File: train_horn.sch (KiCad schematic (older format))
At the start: 72 parts, among them J1 USB_OTG, J2 PROG, Q1 2N7002, SW1 PLAY, U1 MIC7221, U2 MCP73831, U3 TPS78233DDCR, U4 MSP430FR2000_TSSOP, U5 TPA6211A1

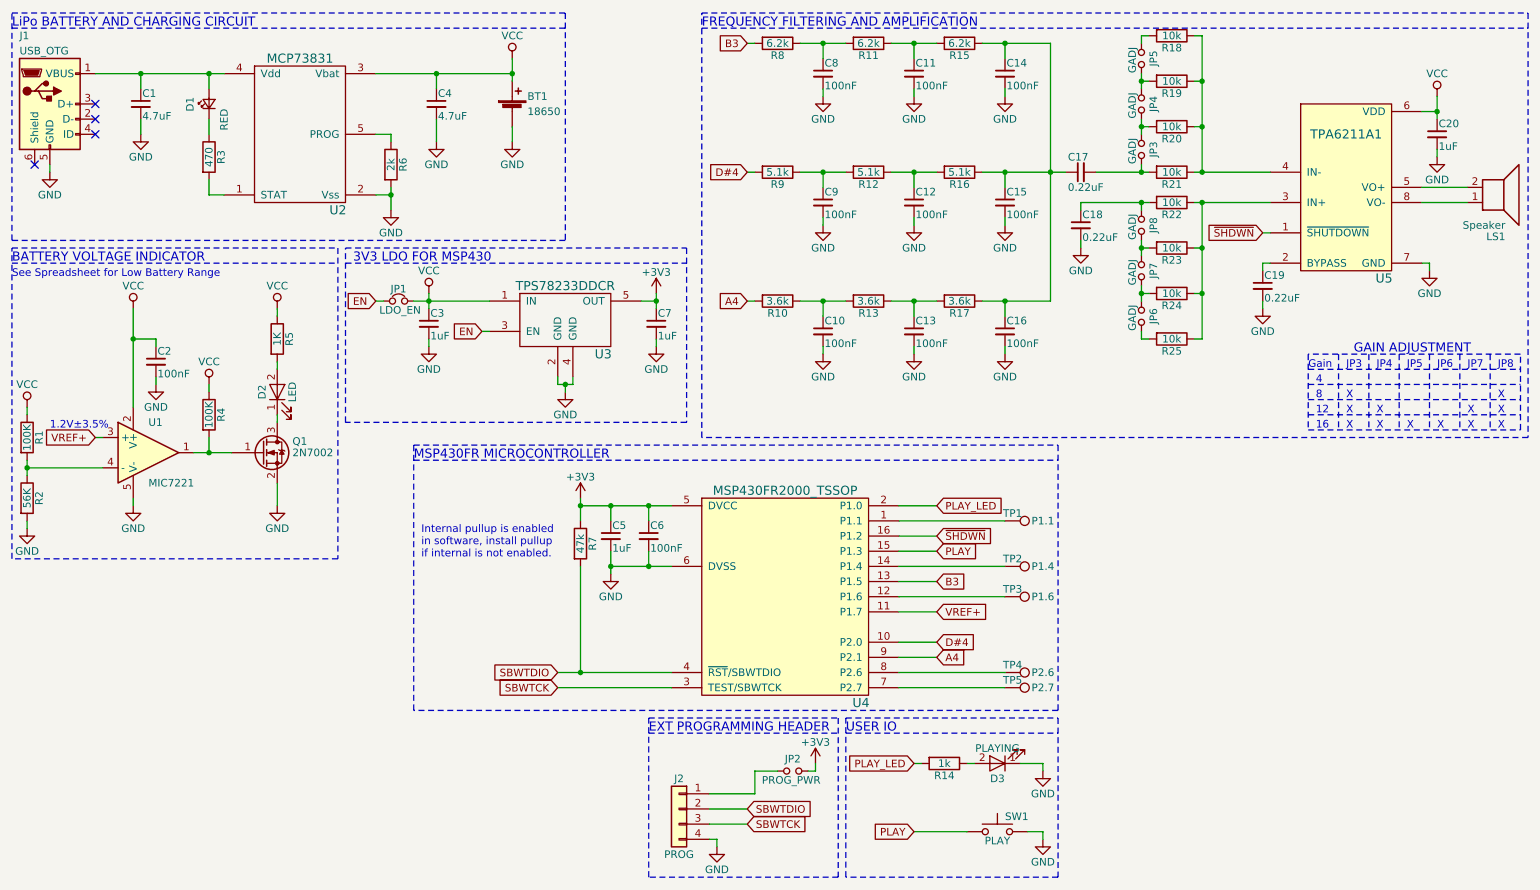
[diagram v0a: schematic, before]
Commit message: update schematic component description fields
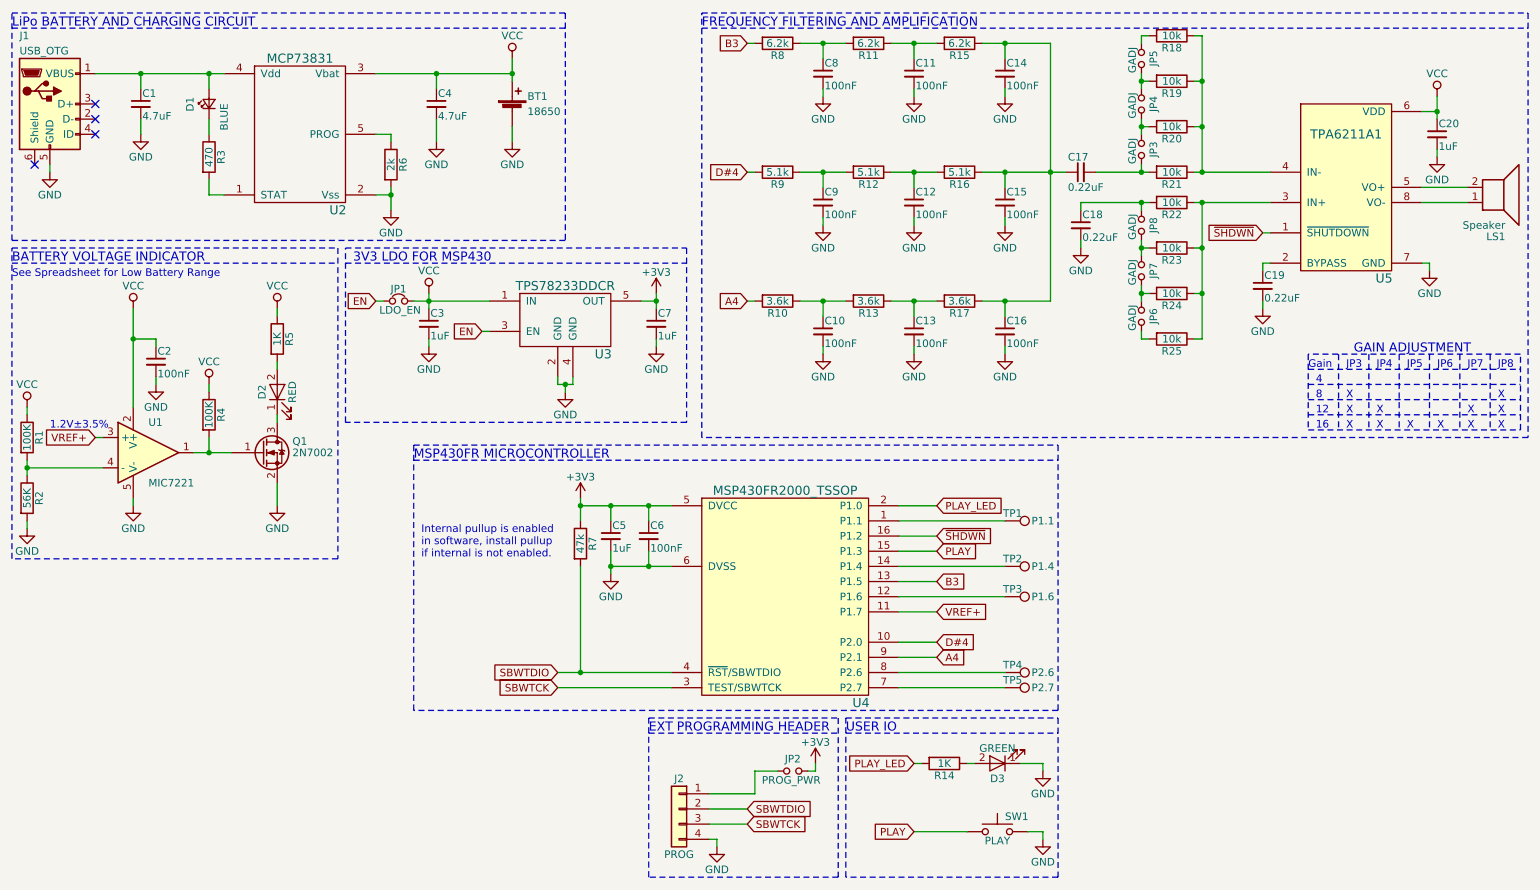
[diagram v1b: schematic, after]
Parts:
- BT1: Description NONE -> HOLDER BATT 18650 1CELL PC PIN; Manufacture NONE -> MPD; Mfg Part Number NONE -> BH-18650-PC-ND; Package NONE -> PC PIN
- C1, C4: Description NONE -> 4.7µF ±10% 6.3V Ceramic Capacitor X5R 0805; Manufacture NONE -> Samsung Electro-Mechanics; Mfg Part Number NONE -> CL21A475KQFNNNG; Package NONE -> 0805
- C10, C2, C6, C8, C9: Description NONE -> CAP CER 0.1UF 16V X7R 0805; Manufacture NONE -> Samsung Electro-Mechanics; Mfg Part Number NONE -> CL21B104KOANNNC; Package NONE -> 0805
- C11, C12, C13, C14, C15, C16: Description (none) -> CAP CER 0.1UF 16V X7R 0805; Manufacture (none) -> Samsung Electro-Mechanics; Mfg Part Number (none) -> CL21B104KOANNNC; Package (none) -> 0805
- C17, C18: Description (none) -> CAP CER 0.22UF 25V X7R 0805; Manufacture (none) -> Samsung Electro-Mechanics; Mfg Part Number (none) -> CL21B224KAFNNNG; Package (none) -> 0805
- C19: Description NONE -> CAP CER 0.22UF 25V X7R 0805; Manufacture NONE -> Samsung Electro-Mechanics; Mfg Part Number NONE -> CL21B224KAFNNNG; Package NONE -> 0805
- C20, C3, C5, C7: Description NONE -> CAP CER 1UF 16V X7R 0805; Manufacture NONE -> Samsung Electro-Mechanics; Mfg Part Number NONE -> CL21B105KOFNNNG; Package NONE -> 0805
- D1: value RED -> BLUE; Description NONE -> Blue 470nm LED Indication; Manufacture NONE -> Wurth Electronics Inc.; Mfg Part Number NONE -> 150080BS75000; Package NONE -> 0805
- D2: value LED -> RED; Description (none) -> LED RED CLEAR 0805 SMD; Manufacture (none) -> Wurth Electronics Inc.; Mfg Part Number (none) -> 150080RS75000; Package (none) -> 0805
- D3: value PLAYING -> GREEN; Description NONE -> LED GREEN CLEAR 0805 SMD; Manufacture NONE -> Wurth Electronics Inc.; Mfg Part Number NONE -> 150080GS75000; Package NONE -> 0805
- J1: Description (none) -> USB - micro B USB 2.0 Receptacle Connector 5 Position Surfa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; Manufacture (none) -> Amphenol; Mfg Part Number (none) -> 10118192-0001LF; Package (none) -> USB MICRO B
- J2: Description NONE -> CONN HEADER 4 POS 2.54; Manufacture NONE -> (none); Mfg Part Number NONE -> (none); Package NONE -> PC PIN
- JP1: Description NONE -> RES SMD 0 OHM JUMPER 1/4W 1206; Manufacture NONE -> Yageo; Mfg Part Number NONE -> RC1206JR-070RL; Package NONE -> 1206
- JP2: Description NONE -> CONN HEADER 2 POS 2.54; Manufacture NONE -> (none); Mfg Part Number NONE -> (none); Package NONE -> PC PIN
- LS1: Description (none) -> 2POS 5MM SCREW TERMINAL BLOCK; Package (none) -> PC PIN
- Q1: Description (none) -> MOSFET N-CH 60V 300MA SOT-23; Manufacture (none) -> Vishay Siliconix; Mfg Part Number (none) -> 2N7002K-T1-E3; Package (none) -> SOT-23
- R1, R4: Description NONE -> RES SMD 100K OHM 1% 1/8W 0805; Manufacture NONE -> Yageo; Mfg Part Number NONE -> RC0805FR-07100KL; Package NONE -> 0805
- R10, R13, R17: Description NONE -> RES SMD 3.6K OHM 0.1% 1/8W 0805; Manufacture NONE -> Panasonic Electronic Components; Mfg Part Number NONE -> ERA-6AEB362V; Package NONE -> 0805
- R11, R15, R8: Description NONE -> RES SMD 6.2K OHM 1% 1/8W 0805; Manufacture NONE -> Yageo; Mfg Part Number NONE -> RC0805FR-076K2L; Package NONE -> 0805
- R12, R16, R9: Description NONE -> RES SMD 5.1K OHM 1% 1/8W 0805; Manufacture NONE -> Yageo; Mfg Part Number NONE -> RC0805FR-075K1L; Package NONE -> 0805
- R14: value 1k -> 1K; Description NONE -> RES SMD 1K OHM 1% 1/8W 0805; Manufacture NONE -> https://www.digikey.com/en/supplier-centers/y/yageo; Mfg Part Number NONE -> RC0805FR-071KL; Package NONE -> 0805
- R18, R19, R20, R21, R22, R23, R24, R25: Description NONE -> RES SMD 10K OHM 1% 1/8W 0805; Manufacture NONE -> Yageo; Mfg Part Number NONE -> RC0805FR-0710KL; Package NONE -> 0805
- R2: Description NONE -> RES SMD 56K OHM 1% 1/8W 0805; Manufacture NONE -> Rohm Semiconductor; Mfg Part Number NONE -> MCR10ERTF5602; Package NONE -> 0805
- R3: Description NONE -> RES SMD 470 OHM 1% 1/8W 0805; Manufacture NONE -> Yageo; Mfg Part Number NONE -> RC0805FR-07470RL; Package NONE -> 0805
- R5: Description NONE -> RES SMD 1K OHM 1% 1/8W 0805; Manufacture NONE -> https://www.digikey.com/en/supplier-centers/y/yageo; Mfg Part Number NONE -> RC0805FR-071KL; Package NONE -> 0805
- R6: Description NONE -> RES SMD 2K OHM 1% 1/8W 0805; Manufacture NONE -> Yageo; Mfg Part Number NONE -> RC0805FR-072KL; Package NONE -> 0805
- R7, TP1, TP2, TP3, TP4, TP5: Description NONE -> (none); Manufacture NONE -> (none); Mfg Part Number NONE -> (none); Package NONE -> (none)
- SW1: Description NONE -> SWITCH TACTILE SPST-NO 0.05A 12V; Manufacture NONE -> Panasonic Electronic Components; Mfg Part Number NONE -> EVQ-P7C01P; Package NONE -> Gull Wing
- U1: Description NONE -> IC COMPARATOR R-R SOT-23-5; Manufacture NONE -> Microchip Technology; Mfg Part Number NONE -> MIC7221YM5-TR; Package NONE -> SOT-23-5
- U3: Description (none) -> IC REG LINEAR 3.3V 150MA SOT23-5; Manufacture (none) -> Texas Instruments; Mfg Part Number (none) -> TPS78233DDCR; Package (none) -> SOT23-5
- U4: Description (none) -> 16 MHZ ULTRA-LOW-POWER MICROCONT; Manufacture (none) -> Texas Instruments; Mfg Part Number (none) -> MSP430FR2000IPW16; Package (none) -> 16-TSSOP
- U5: Description (none) -> IC AMP AUDIO PWR 3.1W MONO 8MSOP; Manufacture (none) -> Texas Instruments; Mfg Part Number (none) -> TPA6211A1DGNR; Package (none) -> 8MSOP

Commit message: clean up component discriptions
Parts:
- C1, C4: Description 4.7µF ±10% 6.3V Ceramic Capacitor X5R 0805 -> CAP CER 4.7UF 6.3V X5R 0805
- J1: Description USB - micro B USB 2.0 Receptacle Connector 5 Position Surfa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 -> CONN USB MICRO B RECPT SMT R/A
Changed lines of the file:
@@
 F 5 "CL21A475KQFNNNG" H 1350 1100 60  0001 C CNN "Mfg Part Number"
 F 6 "0805" H 1350 1100 60  0001 C CNN "Package"
-F 7 "4.7µF ±10% 6.3V Ceramic Capacitor X5R 0805 " H 1350 1100 60  0001 C CNN "Description"
+F 7 "CAP CER 4.7UF 6.3V X5R 0805" H 1350 1100 60  0001 C CNN "Description"
 	1    1350 1100
 	1    0    0    -1
@@
 F 5 "10118192-0001LF" H 750 1100 60  0001 C CNN "Mfg Part Number"
 F 6 "USB MICRO B" H 750 1100 60  0001 C CNN "Package"
-F 7 "USB - micro B USB 2.0 Receptacle Connector 5 Position Surface Mount, Right Angle" H 750 1100 60  0001 C CNN "Description"
+F 7 "CONN USB MICRO B RECPT SMT R/A" H 750 1100 60  0001 C CNN "Description"
 	1    750  1100
 	1    0    0    -1
@@
 F 5 "CL21A475KQFNNNG" H 3300 1100 60  0001 C CNN "Mfg Part Number"
 F 6 "0805" H 3300 1100 60  0001 C CNN "Package"
-F 7 "4.7µF ±10% 6.3V Ceramic Capacitor X5R 0805 " H 3300 1100 60  0001 C CNN "Description"
+F 7 "CAP CER 4.7UF 6.3V X5R 0805" H 3300 1100 60  0001 C CNN "Description"
 	1    3300 1100
 	1    0    0    -1

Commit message: R7 add note in discription not to populate
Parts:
- R7: Description (none) -> DO NOT POPULATE; Manufacture (none) -> NONE; Mfg Part Number (none) -> NONE; Package (none) -> NONE
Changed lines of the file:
@@
 F 2 "Resistors_SMD:R_0805" V 4180 4000 50  0001 C CNN
 F 3 "" H 4250 4000 50  0001 C CNN
+F 4 "NONE" H 4250 4000 60  0001 C CNN "Manufacture"
+F 5 "NONE" H 4250 4000 60  0001 C CNN "Mfg Part Number"
+F 6 "NONE" H 4250 4000 60  0001 C CNN "Package"
+F 7 "DO NOT POPULATE" H 4250 4000 60  0001 C CNN "Description"
 	1    4250 4000
 	1    0    0    -1

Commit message: R10, R13, R17 update from super expensive 0.1% resistor to reasonable 1%
For some reason I chose a super expensive 3.6K 0.1% resistor when all the others are 1%. No need for super presision.
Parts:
- R10, R13, R17: Description RES SMD 3.6K OHM 0.1% 1/8W 0805 -> RES SMD 3.6K OHM 1% 1/8W 0805; Manufacture Panasonic Electronic Components -> Yageo; Mfg Part Number ERA-6AEB362V -> RC0805FR-073K6L
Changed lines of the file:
@@
 F 1 "3.6k" V 5550 2400 50  0000 C CNN
 F 2 "Resistors_SMD:R_0805" V 5480 2400 50  0001 C CNN
-F 3 "https://industrial.panasonic.com/cdbs/www-data/pdf/RDM0000/AOA0000C307.pdf" H 5550 2400 50  0001 C CNN
-F 4 "Panasonic Electronic Components" H 5550 2400 60  0001 C CNN "Manufacture"
-F 5 "ERA-6AEB362V" H 5550 2400 60  0001 C CNN "Mfg Part Number"
+F 3 "http://www.yageo.com/documents/recent/PYu-RC_Group_51_RoHS_L_8.pdf" H 5550 2400 50  0001 C CNN
+F 4 "Yageo" H 5550 2400 60  0001 C CNN "Manufacture"
+F 5 "RC0805FR-073K6L" H 5550 2400 60  0001 C CNN "Mfg Part Number"
 F 6 "0805" H 5550 2400 60  0001 C CNN "Package"
-F 7 "RES SMD 3.6K OHM 0.1% 1/8W 0805" H 5550 2400 60  0001 C CNN "Description"
+F 7 "RES SMD 3.6K OHM 1% 1/8W 0805" H 5550 2400 60  0001 C CNN "Description"
 	1    5550 2400
 	0    1    1    0
@@
 F 1 "3.6k" V 6150 2400 50  0000 C CNN
 F 2 "Resistors_SMD:R_0805" V 6080 2400 50  0001 C CNN
-F 3 "https://industrial.panasonic.com/cdbs/www-data/pdf/RDM0000/AOA0000C307.pdf" H 6150 2400 50  0001 C CNN
-F 4 "Panasonic Electronic Components" H 6150 2400 60  0001 C CNN "Manufacture"
-F 5 "ERA-6AEB362V" H 6150 2400 60  0001 C CNN "Mfg Part Number"
+F 3 "http://www.yageo.com/documents/recent/PYu-RC_Group_51_RoHS_L_8.pdf" H 6150 2400 50  0001 C CNN
+F 4 "Yageo" H 6150 2400 60  0001 C CNN "Manufacture"
+F 5 "RC0805FR-073K6L" H 6150 2400 60  0001 C CNN "Mfg Part Number"
 F 6 "0805" H 6150 2400 60  0001 C CNN "Package"
-F 7 "RES SMD 3.6K OHM 0.1% 1/8W 0805" H 6150 2400 60  0001 C CNN "Description"
+F 7 "RES SMD 3.6K OHM 1% 1/8W 0805" H 6150 2400 60  0001 C CNN "Description"
 	1    6150 2400
 	0    1    1    0
@@
 F 1 "3.6k" V 6750 2400 50  0000 C CNN
 F 2 "Resistors_SMD:R_0805" V 6680 2400 50  0001 C CNN
-F 3 "https://industrial.panasonic.com/cdbs/www-data/pdf/RDM0000/AOA0000C307.pdf" H 6750 2400 50  0001 C CNN
-F 4 "Panasonic Electronic Components" H 6750 2400 60  0001 C CNN "Manufacture"
-F 5 "ERA-6AEB362V" H 6750 2400 60  0001 C CNN "Mfg Part Number"
+F 3 "http://www.yageo.com/documents/recent/PYu-RC_Group_51_RoHS_L_8.pdf" H 6750 2400 50  0001 C CNN
+F 4 "Yageo" H 6750 2400 60  0001 C CNN "Manufacture"
+F 5 "RC0805FR-073K6L" H 6750 2400 60  0001 C CNN "Mfg Part Number"
 F 6 "0805" H 6750 2400 60  0001 C CNN "Package"
-F 7 "RES SMD 3.6K OHM 0.1% 1/8W 0805" H 6750 2400 60  0001 C CNN "Description"
+F 7 "RES SMD 3.6K OHM 1% 1/8W 0805" H 6750 2400 60  0001 C CNN "Description"
 	1    6750 2400
 	0    1    1    0

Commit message: update gain jumper fields
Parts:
- JP3, JP4, JP5, JP6, JP7, JP8: Description NONE -> RES SMD 0 OHM JUMPER 1/4W 1206; Manufacture NONE -> Yageo; Mfg Part Number NONE -> RC1206JR-070RL; Package NONE -> 1206
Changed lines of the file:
@@
 F 1 "GADJ" H 7960 740 50  0000 C CNN
 F 2 "Resistors_SMD:R_1206_HandSoldering" H 7950 800 50  0001 C CNN
-F 3 "" H 7950 800 50  0001 C CNN
-F 4 "NONE" H 7950 800 60  0001 C CNN "Manufacture"
-F 5 "NONE" H 7950 800 60  0001 C CNN "Mfg Part Number"
-F 6 "NONE" H 7950 800 60  0001 C CNN "Package"
-F 7 "NONE" H 7950 800 60  0001 C CNN "Description"
+F 3 "http://www.yageo.com/documents/recent/PYu-RC_Group_51_RoHS_L_8.pdf" H 7950 800 50  0001 C CNN
+F 4 "Yageo" H 7950 800 60  0001 C CNN "Manufacture"
+F 5 "RC1206JR-070RL" H 7950 800 60  0001 C CNN "Mfg Part Number"
+F 6 "1206" H 7950 800 60  0001 C CNN "Package"
+F 7 "RES SMD 0 OHM JUMPER 1/4W 1206" H 7950 800 60  0001 C CNN "Description"
 	1    7950 800
 	0    1    1    0
@@
 F 1 "GADJ" H 7960 1040 50  0000 C CNN
 F 2 "Resistors_SMD:R_1206_HandSoldering" H 7950 1100 50  0001 C CNN
-F 3 "" H 7950 1100 50  0001 C CNN
-F 4 "NONE" H 7950 1100 60  0001 C CNN "Manufacture"
-F 5 "NONE" H 7950 1100 60  0001 C CNN "Mfg Part Number"
-F 6 "NONE" H 7950 1100 60  0001 C CNN "Package"
-F 7 "NONE" H 7950 1100 60  0001 C CNN "Description"
+F 3 "http://www.yageo.com/documents/recent/PYu-RC_Group_51_RoHS_L_8.pdf" H 7950 1100 50  0001 C CNN
+F 4 "Yageo" H 7950 1100 60  0001 C CNN "Manufacture"
+F 5 "RC1206JR-070RL" H 7950 1100 60  0001 C CNN "Mfg Part Number"
+F 6 "1206" H 7950 1100 60  0001 C CNN "Package"
+F 7 "RES SMD 0 OHM JUMPER 1/4W 1206" H 7950 1100 60  0001 C CNN "Description"
 	1    7950 1100
 	0    1    1    0
@@
 F 1 "GADJ" H 7960 1340 50  0000 C CNN
 F 2 "Resistors_SMD:R_1206_HandSoldering" H 7950 1400 50  0001 C CNN
-F 3 "" H 7950 1400 50  0001 C CNN
-F 4 "NONE" H 7950 1400 60  0001 C CNN "Manufacture"
-F 5 "NONE" H 7950 1400 60  0001 C CNN "Mfg Part Number"
-F 6 "NONE" H 7950 1400 60  0001 C CNN "Package"
-F 7 "NONE" H 7950 1400 60  0001 C CNN "Description"
+F 3 "http://www.yageo.com/documents/recent/PYu-RC_Group_51_RoHS_L_8.pdf" H 7950 1400 50  0001 C CNN
+F 4 "Yageo" H 7950 1400 60  0001 C CNN "Manufacture"
+F 5 "RC1206JR-070RL" H 7950 1400 60  0001 C CNN "Mfg Part Number"
+F 6 "1206" H 7950 1400 60  0001 C CNN "Package"
+F 7 "RES SMD 0 OHM JUMPER 1/4W 1206" H 7950 1400 60  0001 C CNN "Description"
 	1    7950 1400
 	0    1    1    0
@@
 F 1 "GADJ" H 7960 1840 50  0000 C CNN
 F 2 "Resistors_SMD:R_1206_HandSoldering" H 7950 1900 50  0001 C CNN
-F 3 "" H 7950 1900 50  0001 C CNN
-F 4 "NONE" H 7950 1900 60  0001 C CNN "Manufacture"
-F 5 "NONE" H 7950 1900 60  0001 C CNN "Mfg Part Number"
-F 6 "NONE" H 7950 1900 60  0001 C CNN "Package"
-F 7 "NONE" H 7950 1900 60  0001 C CNN "Description"
+F 3 "http://www.yageo.com/documents/recent/PYu-RC_Group_51_RoHS_L_8.pdf" H 7950 1900 50  0001 C CNN
+F 4 "Yageo" H 7950 1900 60  0001 C CNN "Manufacture"
+F 5 "RC1206JR-070RL" H 7950 1900 60  0001 C CNN "Mfg Part Number"
+F 6 "1206" H 7950 1900 60  0001 C CNN "Package"
+F 7 "RES SMD 0 OHM JUMPER 1/4W 1206" H 7950 1900 60  0001 C CNN "Description"
 	1    7950 1900
 	0    1    1    0
@@
 F 1 "GADJ" H 7960 2140 50  0000 C CNN
 F 2 "Resistors_SMD:R_1206_HandSoldering" H 7950 2200 50  0001 C CNN
-F 3 "" H 7950 2200 50  0001 C CNN
-F 4 "NONE" H 7950 2200 60  0001 C CNN "Manufacture"
-F 5 "NONE" H 7950 2200 60  0001 C CNN "Mfg Part Number"
-F 6 "NONE" H 7950 2200 60  0001 C CNN "Package"
-F 7 "NONE" H 7950 2200 60  0001 C CNN "Description"
+F 3 "http://www.yageo.com/documents/recent/PYu-RC_Group_51_RoHS_L_8.pdf" H 7950 2200 50  0001 C CNN
+F 4 "Yageo" H 7950 2200 60  0001 C CNN "Manufacture"
+F 5 "RC1206JR-070RL" H 7950 2200 60  0001 C CNN "Mfg Part Number"
+F 6 "1206" H 7950 2200 60  0001 C CNN "Package"
+F 7 "RES SMD 0 OHM JUMPER 1/4W 1206" H 7950 2200 60  0001 C CNN "Description"
 	1    7950 2200
 	0    1    1    0
@@
 F 1 "GADJ" H 7960 2440 50  0000 C CNN
 F 2 "Resistors_SMD:R_1206_HandSoldering" H 7950 2500 50  0001 C CNN
-F 3 "" H 7950 2500 50  0001 C CNN
-F 4 "NONE" H 7950 2500 60  0001 C CNN "Manufacture"
-F 5 "NONE" H 7950 2500 60  0001 C CNN "Mfg Part Number"
-F 6 "NONE" H 7950 2500 60  0001 C CNN "Package"
-F 7 "NONE" H 7950 2500 60  0001 C CNN "Description"
+F 3 "http://www.yageo.com/documents/recent/PYu-RC_Group_51_RoHS_L_8.pdf" H 7950 2500 50  0001 C CNN
+F 4 "Yageo" H 7950 2500 60  0001 C CNN "Manufacture"
+F 5 "RC1206JR-070RL" H 7950 2500 60  0001 C CNN "Mfg Part Number"
+F 6 "1206" H 7950 2500 60  0001 C CNN "Package"
+F 7 "RES SMD 0 OHM JUMPER 1/4W 1206" H 7950 2500 60  0001 C CNN "Description"
 	1    7950 2500
 	0    1    1    0

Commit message: fix manufacture name in descriptions
R5 and R14 had links instead of names in the manufacture description fields
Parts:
- R14, R5: Manufacture https://www.digikey.com/en/supplier-centers/y/yageo -> Yageo
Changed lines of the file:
@@
 F 2 "Resistors_SMD:R_0805" V 2180 2650 50  0001 C CNN
 F 3 "http://www.yageo.com/documents/recent/PYu-RC_Group_51_RoHS_L_8.pdf" H 2250 2650 50  0001 C CNN
-F 4 "https://www.digikey.com/en/supplier-centers/y/yageo" H 2250 2650 60  0001 C CNN "Manufacture"
+F 4 "Yageo" H 2250 2650 60  0001 C CNN "Manufacture"
 F 5 "RC0805FR-071KL" H 2250 2650 60  0001 C CNN "Mfg Part Number"
 F 6 "0805" H 2250 2650 60  0001 C CNN "Package"
@@
 F 2 "Resistors_SMD:R_0805" V 6580 5450 50  0001 C CNN
 F 3 "http://www.yageo.com/documents/recent/PYu-RC_Group_51_RoHS_L_8.pdf" H 6650 5450 50  0001 C CNN
-F 4 "https://www.digikey.com/en/supplier-centers/y/yageo" H 6650 5450 60  0001 C CNN "Manufacture"
+F 4 "Yageo" H 6650 5450 60  0001 C CNN "Manufacture"
 F 5 "RC0805FR-071KL" H 6650 5450 60  0001 C CNN "Mfg Part Number"
 F 6 "0805" H 6650 5450 60  0001 C CNN "Package"

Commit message: MCP7383 missing fields filled
MCP7383 info fields were not filled out, corrected with porper info
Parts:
- U2: Description (none) -> IC CONTROLLR LI-ION 4.2V SOT23-5; Manufacture (none) -> Microchip Technology; Mfg Part Number (none) -> MCP73831T-2ACI/OT; Package (none) -> SOT23-5
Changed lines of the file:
@@
 F 1 "MCP73831" H 2400 1800 60  0000 C CNN
 F 2 "TO_SOT_Packages_SMD:SOT-23-5" H 2400 1300 60  0001 C CNN
-F 3 "" H 2400 1300 60  0001 C CNN
+F 3 "http://ww1.microchip.com/downloads/en/DeviceDoc/20001984g.pdf" H 2400 1300 60  0001 C CNN
+F 4 "Microchip Technology" H 2400 1300 60  0001 C CNN "Manufacture"
+F 5 "MCP73831T-2ACI/OT" H 2400 1300 60  0001 C CNN "Mfg Part Number"
+F 6 "SOT23-5" H 2400 1300 60  0001 C CNN "Package"
+F 7 "IC CONTROLLR LI-ION 4.2V SOT23-5" H 2400 1300 60  0001 C CNN "Description"
 	1    2400 1300
 	1    0    0    -1

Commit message: blue led description style same as all components
style points +1
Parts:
- D1: Description Blue 470nm LED Indication -> LED BLUE CLEAR 0805 SMD
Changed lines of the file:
@@
 F 5 "150080BS75000" H 1800 1100 60  0001 C CNN "Mfg Part Number"
 F 6 "0805" H 1800 1100 60  0001 C CNN "Package"
-F 7 "Blue 470nm LED Indication" H 1800 1100 60  0001 C CNN "Description"
+F 7 "LED BLUE CLEAR 0805 SMD" H 1800 1100 60  0001 C CNN "Description"
 	1    1800 1100
 	0    -1   -1   0
